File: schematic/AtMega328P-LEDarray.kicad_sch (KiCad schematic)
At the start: 25 parts, among them J1 JTAG IDC-10, U1 ATmega328-P

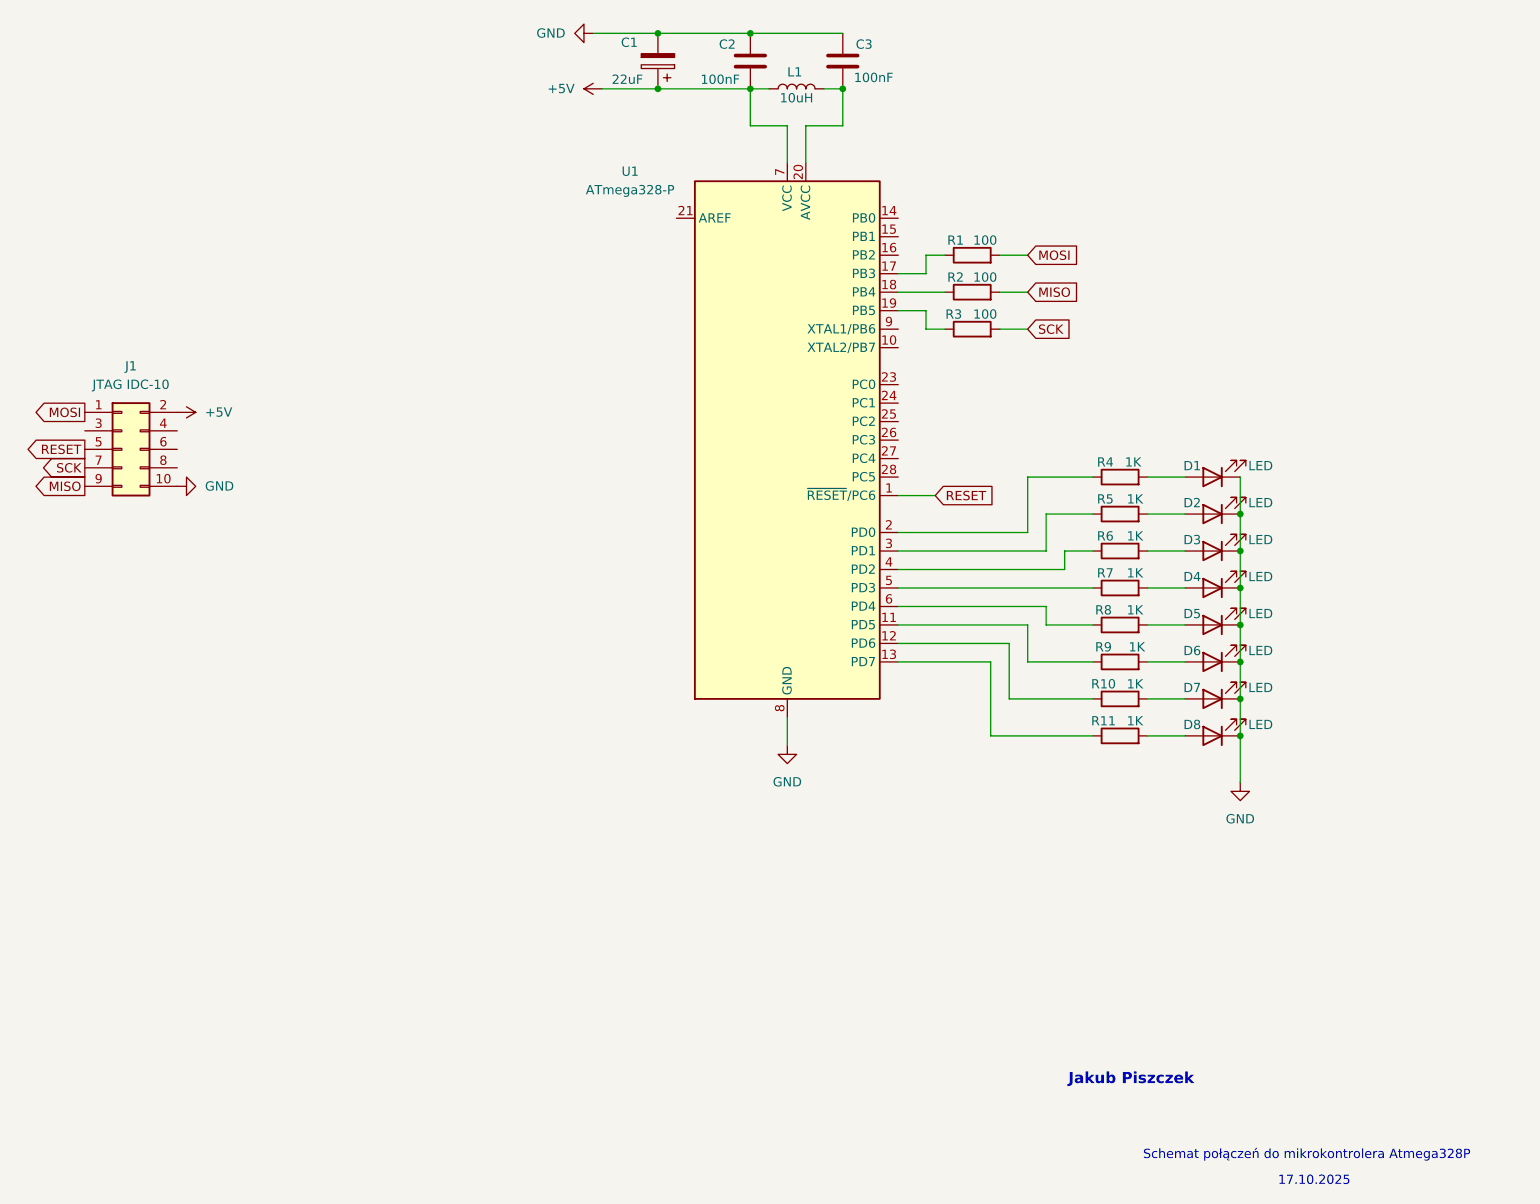
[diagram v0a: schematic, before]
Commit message: button connection added to the diagram
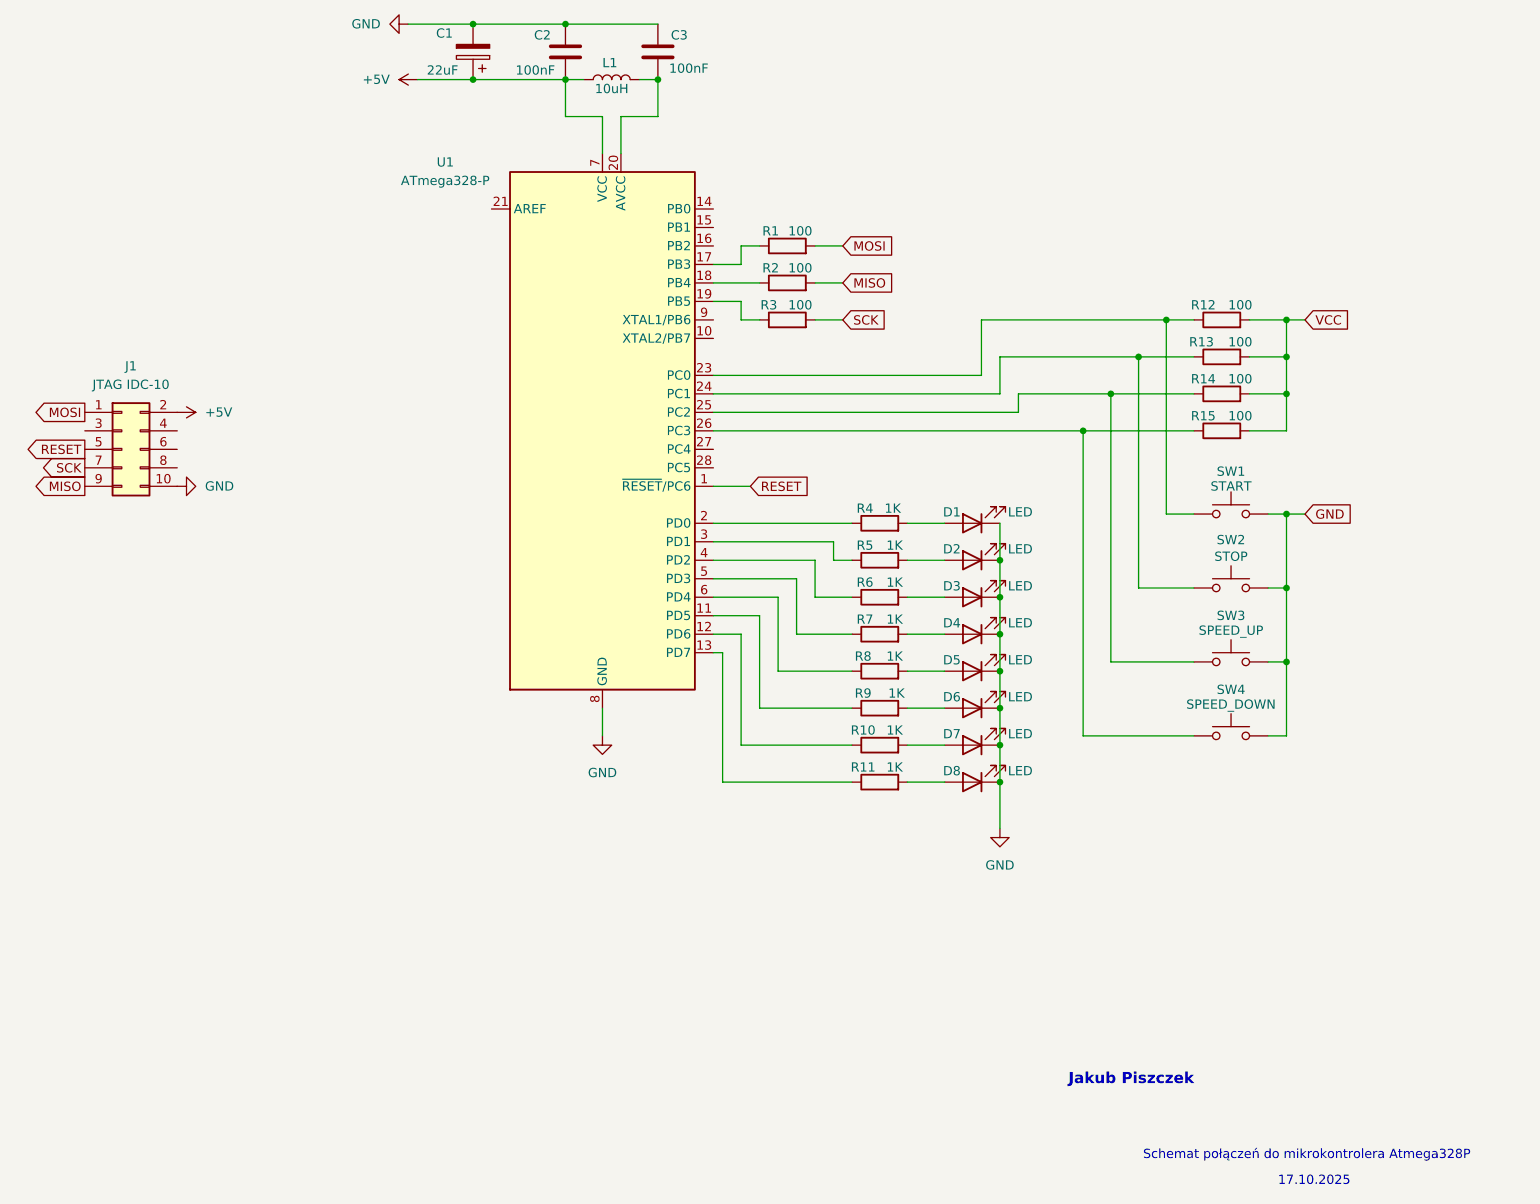
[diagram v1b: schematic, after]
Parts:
- added R12, R13, R14, R15: 100, symbol Device:R
- added SW1: START, symbol Switch:SW_Push
- added SW2: STOP, symbol Switch:SW_Push
- added SW3: SPEED_UP, symbol Switch:SW_Push
- added SW4: SPEED_DOWN, symbol Switch:SW_Push
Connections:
- net GND: now also SW1.2, SW2.2, SW3.2, SW4.2
- net at U1.23 (PC0): now also R12.1, SW1.1
- net at U1.24 (PC1): now also R13.1, SW2.1
- net at U1.25 (PC2): now also R14.1, SW3.1
- net at U1.26 (PC3): now also R15.1, SW4.1
- new net VCC: R12.2, R13.2, R14.2, R15.2
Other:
- moved on the sheet: C1, C2, C3, D1, D2, D3, D4, D5, D6, D7, D8, L1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
